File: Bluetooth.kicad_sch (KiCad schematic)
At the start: 5 parts, among them U10 RN4871-I, U9 MCP112

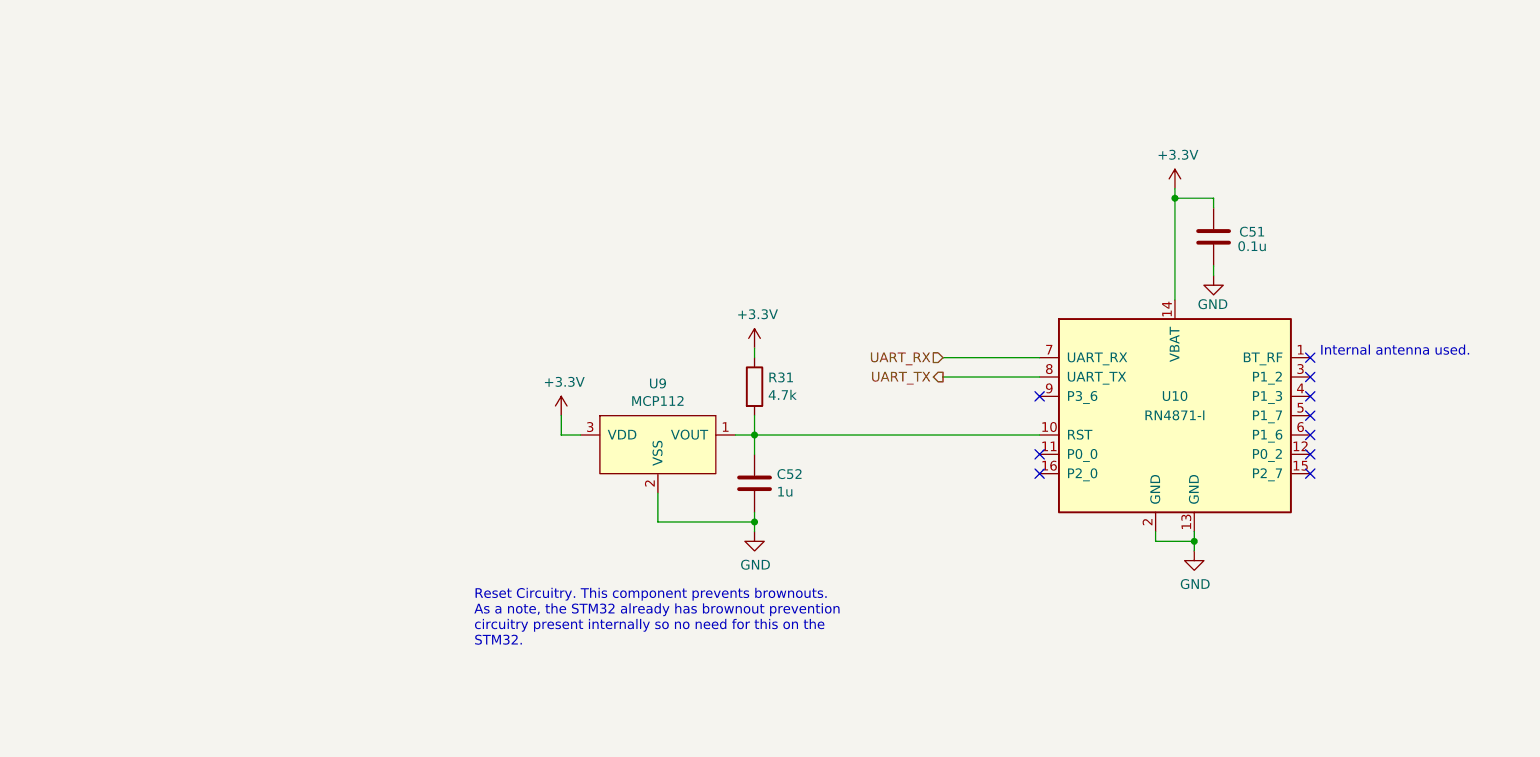
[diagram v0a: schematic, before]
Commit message: new bt module + preliminary reverse protection
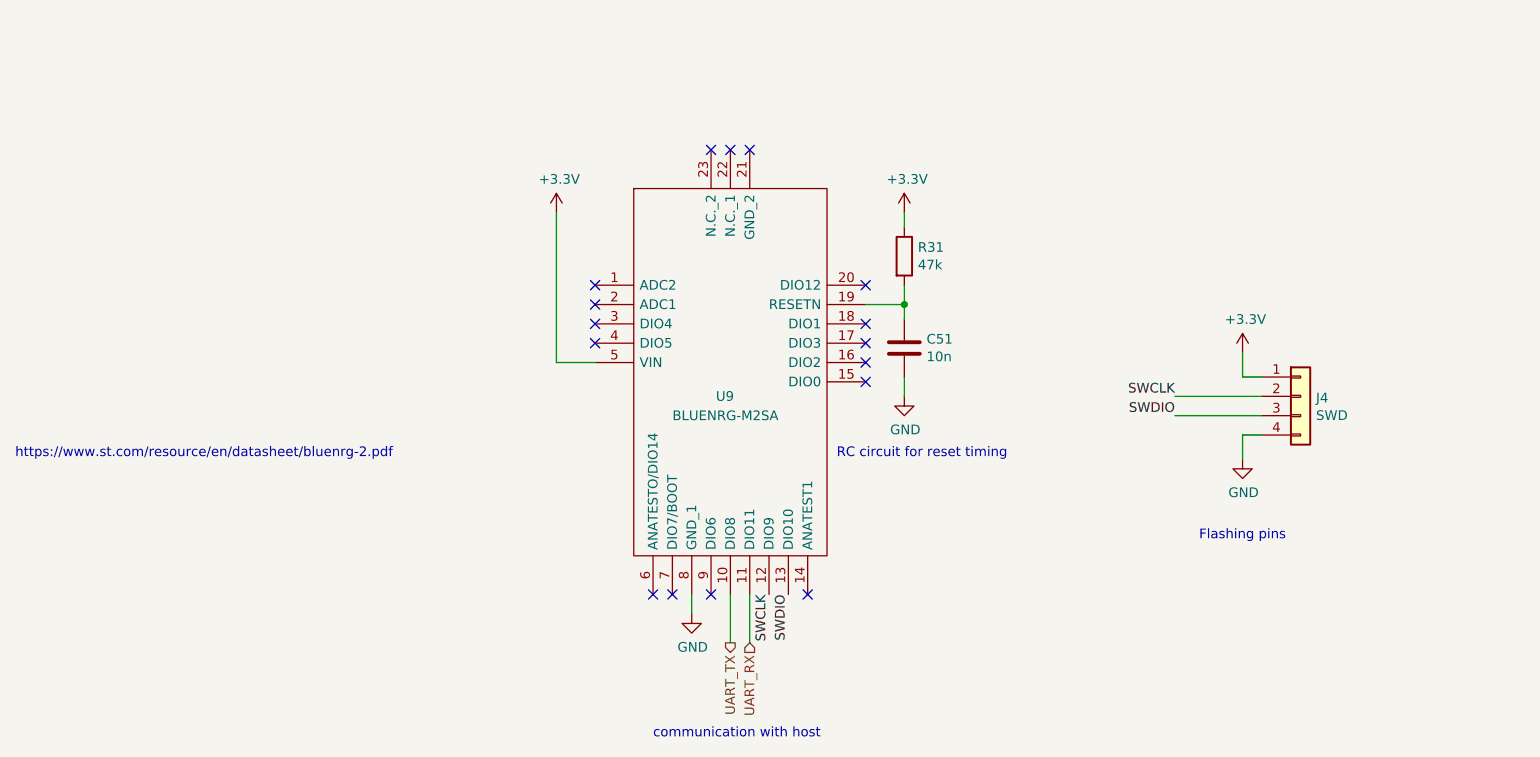
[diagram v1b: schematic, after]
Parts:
- removed C51: 0.1u, Capacitor_SMD:C_0805_2012Metric, symbol Device:C
- removed U10: RN4871-I, RF_Module:Microchip_RN4871, symbol RF_Bluetooth:RN4871
- removed U9: MCP112, Package_TO_SOT_SMD:SOT-23, symbol utsvt-bps:MCP112
- added J4: SWD, Connector_PinHeader_2.54mm:PinHeader_1x04_P2.54mm_Vertical, symbol Connector_Generic:Conn_01x04
- added U9: BLUENRG-M2SA, BLUENRGM2SA, symbol BLUENRG-M2SA:BLUENRG-M2SA
- C51: renamed from C52; value 1u -> 10n
- R31: value 4.7k -> 47k
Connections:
- net +3.3V: now also J4.1 (Pin_1), U9.5 (VIN)
- net GND: now also J4.4 (Pin_4), U9.8 (GND_1)
- net UART_RX: now also U9.11 (DIO11)
- net UART_TX: now also U9.10 (DIO8)
- net at C51.1, R31.2: now also U9.19 (RESETN)
- new net SWCLK: J4.2 (Pin_2), U9.12 (DIO9)
- new net SWDIO: J4.3 (Pin_3), U9.13 (DIO10)
- no-connect marks 10 -> 16
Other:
- note added: "Flashing pins"
- note added: "RC circuit for reset timing"
- note added: "communication with host"
- note added: "https://www.st.com/resource/en/datasheet/bluenrg-2.pdf"
- note removed: "Internal antenna used."
- note removed: "Reset Circuitry. This component prevents brownouts. As a note, the STM32 already has brownout prevention circuitry present internally so no need for this on the STM32."
- moved on the sheet: C51, R31

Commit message: basic inputs
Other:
- note added: "SOC datasheet"
- note removed: "https://www.st.com/resource/en/datasheet/bluenrg-2.pdf"
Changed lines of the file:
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@@
     (effects (font (size 1.27 1.27)) (justify left bottom))
   )
-  (text "https://www.st.com/resource/en/datasheet/bluenrg-2.pdf"
-    (at 25.4 99.695 0)
+  (text "SOC datasheet" (at 112.395 97.155 0)
     (effects (font (size 1.27 1.27)) (justify left bottom) (href "https://www.st.com/resource/en/datasheet/bluenrg-2.pdf"))
   )

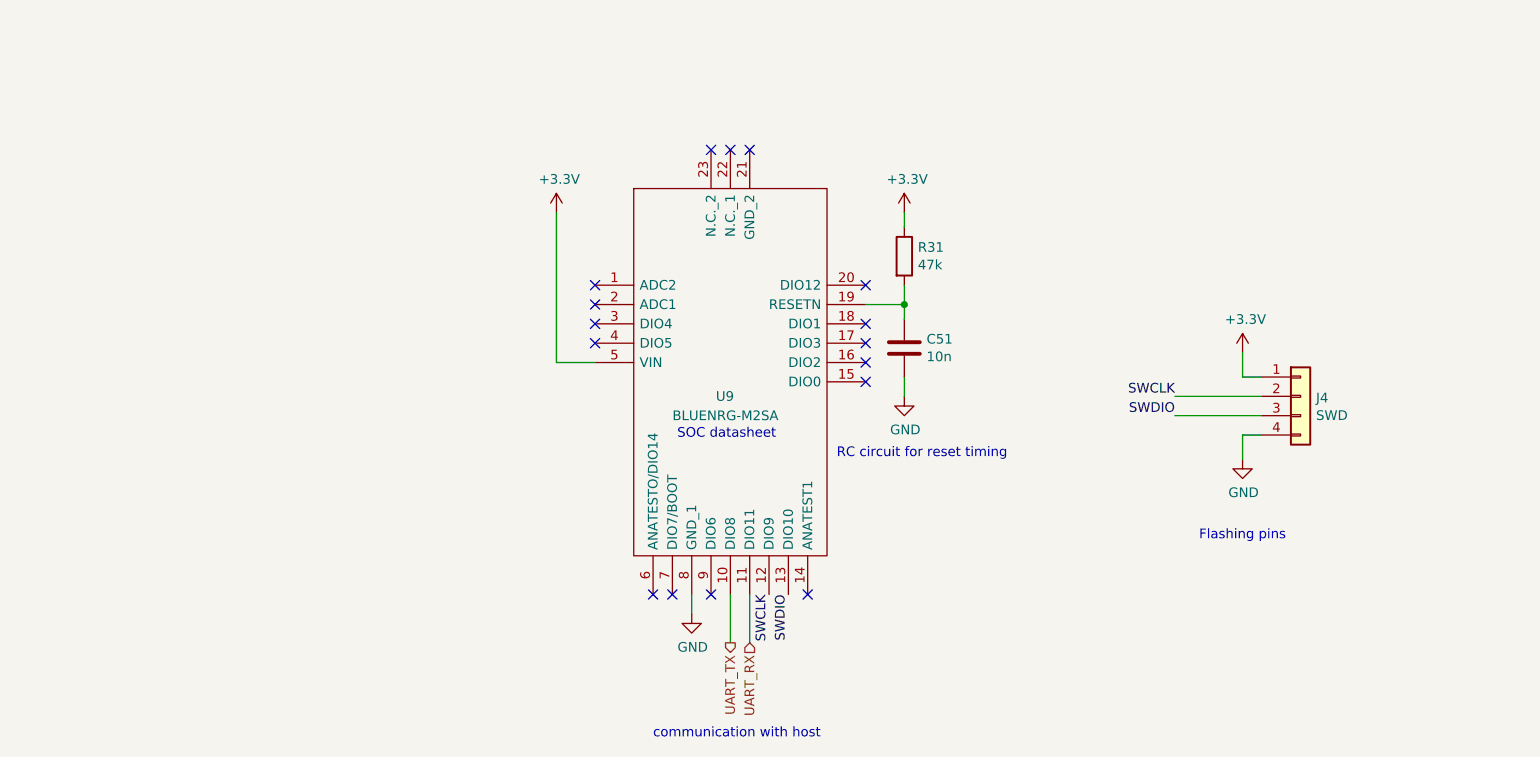
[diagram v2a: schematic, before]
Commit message: switch changes, some caps, annotations
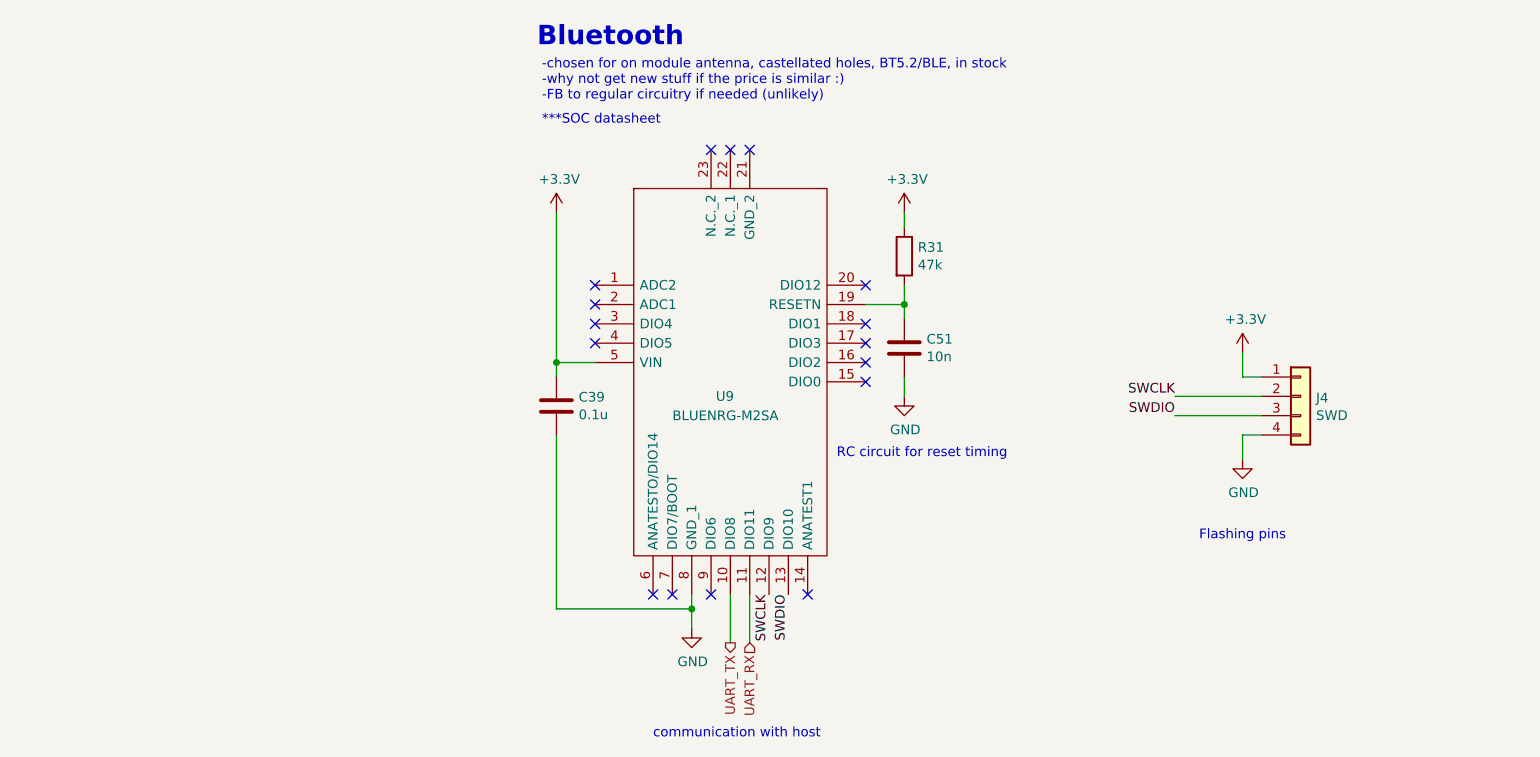
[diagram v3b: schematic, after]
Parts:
- added C39: 0.1u, Capacitor_SMD:C_0805_2012Metric, symbol Device:C
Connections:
- net +3.3V: now also C39.1
- net GND: now also C39.2
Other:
- note added: "***SOC datasheet"
- note added: "-chosen for on module antenna, castellated holes, BT5.2/BLE, in stock -why not get new stuff if the price is similar :) -FB to regular circuitry if needed (unlikely)"
- note added: "Bluetooth"
- note removed: "SOC datasheet"
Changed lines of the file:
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@@
 (kicad_sch (version 20230121) (generator eeschema)
   (paper "A4")
+  (junction (at 96.52 86.995) (diameter 0) (color 0 0 0 0)
+  )
   (junction (at 142.24 79.375) (diameter 0) (color 0 0 0 0)
+  )
+  (junction (at 114.3 119.38) (diameter 0) (color 0 0 0 0)
   )
   (no_connect (at 101.6 81.915))
@@
     (stroke (width 0) (type default))
   )
+  (wire (pts (xy 96.52 119.38) (xy 96.52 96.52))
+    (stroke (width 0) (type default))
+  )
   (wire (pts (xy 177.8 93.98) (xy 189.23 93.98))
     (stroke (width 0) (type default))
@@
     (stroke (width 0) (type default))
   )
+  (wire (pts (xy 114.3 119.38) (xy 114.3 121.92))
+    (stroke (width 0) (type default))
+  )
+  (wire (pts (xy 96.52 86.995) (xy 96.52 88.9))
+    (stroke (width 0) (type default))
+  )
   (wire (pts (xy 186.69 99.695) (xy 186.69 96.52))
     (stroke (width 0) (type default))
@@
     (stroke (width 0) (type default))
   )
+  (wire (pts (xy 114.3 119.38) (xy 96.52 119.38))
+    (stroke (width 0) (type default))
+  )
   (wire (pts (xy 96.52 86.995) (xy 101.6 86.995))
     (stroke (width 0) (type default))
   )
-  (wire (pts (xy 114.3 117.475) (xy 114.3 120.015))
+  (wire (pts (xy 114.3 117.475) (xy 114.3 119.38))
     (stroke (width 0) (type default))
   )
@@
     (effects (font (size 1.27 1.27)) (justify left bottom))
   )
+  (text "-chosen for on module antenna, castellated holes, BT5.2/BLE, in stock\n-why not get new stuff if the price is similar :)\n-FB to regular circuitry if needed (unlikely)"
+    (at 94.615 52.705 0)
+    (effects (font (size 1.27 1.27)) (justify left bottom))
+  )
   (text "communication with host" (at 109.22 136.525 0)
     (effects (font (size 1.27 1.27)) (justify left bottom))
   )
-  (text "SOC datasheet" (at 112.395 97.155 0)
+  (text "Bluetooth" (at 93.98 45.72 0)
+    (effects (font (size 2.54 2.54) (thickness 0.508) bold) (justify left bottom))
+  )
+  (text "***SOC datasheet" (at 94.615 55.88 0)
     (effects (font (size 1.27 1.27)) (justify left bottom) (href "https://www.st.com/resource/en/datasheet/bluenrg-2.pdf"))
   )
@@
   (hierarchical_label "UART_RX" (shape input) (at 121.92 123.825 270) (fields_autoplaced)
     (effects (font (size 1.27 1.27)) (justify right))
+  )
+  (symbol (lib_id "Device:C") (at 96.52 92.71 0) (unit 1)
+    (in_bom yes) (on_board yes) (dnp no)
+    (property "Reference" "C39" (at 99.441 91.5416 0)
+      (effects (font (size 1.27 1.27)) (justify left))
+    )
+    (property "Value" "0.1u" (at 99.441 93.853 0)
+      (effects (font (size 1.27 1.27)) (justify left))
+    )
+    (property "Footprint" "Capacitor_SMD:C_0805_2012Metric" (at 97.4852 96.52 0)
+      (effects (font (size 1.27 1.27)) hide)
+    )
+    (property "Datasheet" "https://www.mouser.com/datasheet/2/212/KEM_C1002_X7R_SMD-1102033.pdf" (at 96.52 92.71 0)
+      (effects (font (size 1.27 1.27)) hide)
+    )
+    (property "P/N" "C0805C104K5RAC7411" (at 96.52 92.71 0)
+      (effects (font (size 1.27 1.27)) hide)
+    )
+    (pin "1")
+    (pin "2")
+    (instances
+      (project "Telemetry-Primary"
+        (path "/7f2a449b-14af-42b3-8d38-5f0f8a5ee7ce/00000000-0000-0000-0000-00005f6dd18a"
+          (reference "C39") (unit 1)
+        )
+        (path "/7f2a449b-14af-42b3-8d38-5f0f8a5ee7ce/57884461-52ec-4fdf-8849-cb39fe7f004b"
+          (reference "C62") (unit 1)
+        )
+      )
+    )
   )
   (symbol (lib_id "Device:R") (at 142.24 73.025 0) (unit 1)
@@
     )
   )
-  (symbol (lib_id "power:GND") (at 114.3 120.015 0) (unit 1)
-    (in_bom yes) (on_board yes) (dnp no)
-    (property "Reference" "#PWR028" (at 114.3 126.365 0)
-      (effects (font (size 1.27 1.27)) hide)
-    )
-    (property "Value" "GND" (at 114.427 124.4092 0)
-      (effects (font (size 1.27 1.27)))
-    )
-    (property "Footprint" "" (at 114.3 120.015 0)
-      (effects (font (size 1.27 1.27)) hide)
-    )
-    (property "Datasheet" "" (at 114.3 120.015 0)
-      (effects (font (size 1.27 1.27)) hide)
-    )
+  (symbol (lib_id "power:GND") (at 114.3 121.92 0) (unit 1)
+    (in_bom yes) (on_board yes) (dnp no)
+    (property "Reference" "#PWR028" (at 114.3 128.27 0)
+      (effects (font (size 1.27 1.27)) hide)
+    )
+    (property "Value" "GND" (at 114.427 126.3142 0)
+      (effects (font (size 1.27 1.27)))
+    )
+    (property "Footprint" "" (at 114.3 121.92 0)
+      (effects (font (size 1.27 1.27)) hide)
+    )
+    (property "Datasheet" "" (at 114.3 121.92 0)
+      (effects (font (size 1.27 1.27)) hide)
+    )
